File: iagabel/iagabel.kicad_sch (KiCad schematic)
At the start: 17 parts, among them J1 A2008WR-S-4P, K1 TCUT1300X01, U1 74LVC2G14GW

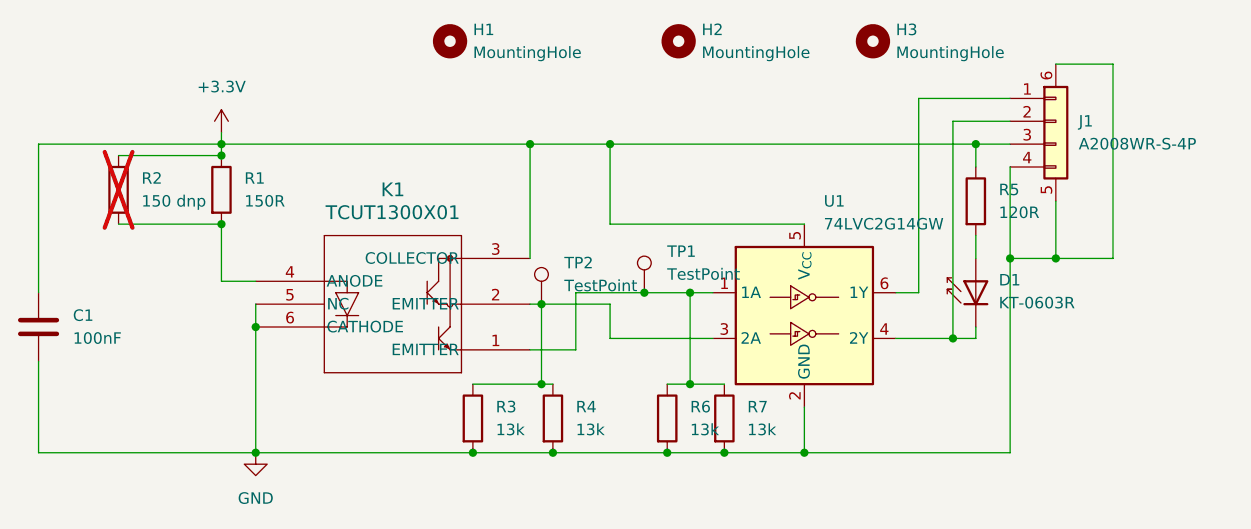
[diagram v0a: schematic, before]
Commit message: iagabel v0.2: changed indicator led resistor to 470 Ohms, production data
I changed the led resistor to 470 ohm because the led was too bright.
For the production run at jlcpcb i designed a panel with mousebites.
The production at jlcpcb started at 16.9.2025
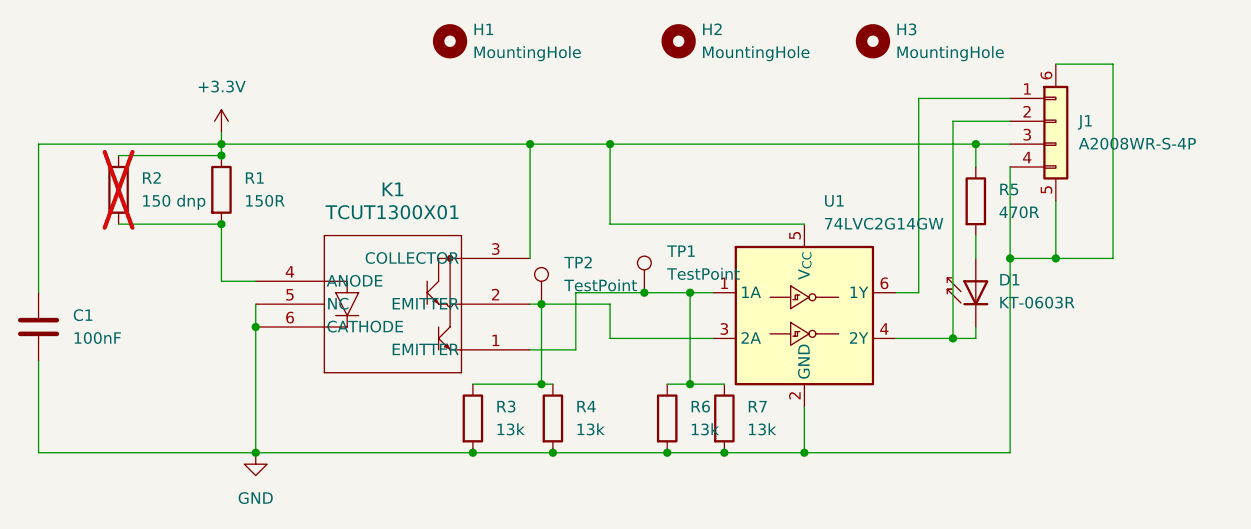
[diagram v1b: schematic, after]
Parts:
- R5: value 120R -> 470R; footprint Resistor_SMD:R_0805_2012Metric -> Resistor_SMD:R_0603_1608Metric; LCSC part number C17437 -> C23179
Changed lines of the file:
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@@
 	(title_block
 		(title "IA - Gabellichtschranke")
-		(date "2025-07-08")
-		(rev "v0.1")
+		(date "2025-08-08")
+		(rev "v0.2")
 		(company "Technische Hochschule Augsburg")
 		(comment 1 "Friedrich Beckmann")
@@
 			)
 		)
-		(property "Value" "120R"
+		(property "Value" "470R"
 			(at 154.94 66.0399 0)
 			(effects
@@
 			)
 		)
-		(property "Footprint" "Resistor_SMD:R_0805_2012Metric"
+		(property "Footprint" "Resistor_SMD:R_0603_1608Metric"
 			(at 150.622 64.77 90)
 			(effects
@@
 			)
 		)
-		(property "Datasheet" "https://jlcpcb.com/api/file/downloadByFileSystemAccessId/8579706485296709632"
+		(property "Datasheet" "https://jlcpcb.com/api/file/downloadByFileSystemAccessId/8579706265439817728"
 			(at 152.4 64.77 0)
 			(effects
@@
 			)
 		)
-		(property "Description" "UNIROYAL 0805W8F1200T5E 0805 120 Ohm"
+		(property "Description" "UNIROYAL 0603WAF4700T5E 0602 470 Ohm"
 			(at 152.4 64.77 0)
 			(effects
@@
 			)
 		)
-		(property "LCSC part number" "C17437"
+		(property "LCSC part number" "C23179"
 			(at 152.4 64.77 0)
 			(effects
